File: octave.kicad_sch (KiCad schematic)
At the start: 24 parts, among them Q3 2N3904, Q4 2N3904, Q5 2N3904

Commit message: Actualización de esquemáticos
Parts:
- R10, R11, R12, R13, R14, R15, R16, R17, R18, R19, R2*, R20, R21, R3*: footprint (none) -> Resistor_THT:R_Axial_DIN0207_L6.3mm_D2.5mm_P7.62mm_Horizontal
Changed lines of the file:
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@@
 (kicad_sch
-	(version 20231120)
+	(version 20250114)
 	(generator "eeschema")
-	(generator_version "8.0")
+	(generator_version "9.0")
 	(paper "A4")
 	(junction
@@
 			)
 		)
-		(property "Footprint" ""
+		(property "Footprint" "Resistor_THT:R_Axial_DIN0207_L6.3mm_D2.5mm_P7.62mm_Horizontal"
 			(at 141.732 86.36 90)
 			(effects
@@
 			)
 		)
-		(property "Footprint" ""
+		(property "Footprint" "Resistor_THT:R_Axial_DIN0207_L6.3mm_D2.5mm_P7.62mm_Horizontal"
 			(at 182.372 59.69 90)
 			(effects
@@
 			)
 		)
-		(property "Footprint" ""
+		(property "Footprint" "Resistor_THT:R_Axial_DIN0207_L6.3mm_D2.5mm_P7.62mm_Horizontal"
 			(at 132.08 76.962 90)
 			(effects
@@
 			)
 		)
-		(property "Footprint" ""
+		(property "Footprint" "Resistor_THT:R_Axial_DIN0207_L6.3mm_D2.5mm_P7.62mm_Horizontal"
 			(at 141.732 137.16 90)
 			(effects
@@
 			)
 		)
-		(property "Footprint" ""
+		(property "Footprint" "Resistor_THT:R_Axial_DIN0207_L6.3mm_D2.5mm_P7.62mm_Horizontal"
 			(at 77.978 113.03 90)
 			(effects
@@
 			)
 		)
-		(property "Footprint" ""
+		(property "Footprint" "Resistor_THT:R_Axial_DIN0207_L6.3mm_D2.5mm_P7.62mm_Horizontal"
 			(at 132.08 127.762 90)
 			(effects
@@
 			)
 		)
-		(property "Footprint" ""
+		(property "Footprint" "Resistor_THT:R_Axial_DIN0207_L6.3mm_D2.5mm_P7.62mm_Horizontal"
 			(at 100.838 71.12 90)
 			(effects
@@
 			)
 		)
-		(property "Footprint" ""
+		(property "Footprint" "Resistor_THT:R_Axial_DIN0207_L6.3mm_D2.5mm_P7.62mm_Horizontal"
 			(at 141.732 123.19 90)
 			(effects
@@
 			)
 		)
-		(property "Footprint" ""
+		(property "Footprint" "Resistor_THT:R_Axial_DIN0207_L6.3mm_D2.5mm_P7.62mm_Horizontal"
 			(at 230.378 80.01 90)
 			(effects
@@
 			)
 		)
-		(property "Footprint" ""
+		(property "Footprint" "Resistor_THT:R_Axial_DIN0207_L6.3mm_D2.5mm_P7.62mm_Horizontal"
 			(at 113.538 71.12 90)
 			(effects
@@
 			)
 		)
-		(property "Footprint" ""
+		(property "Footprint" "Resistor_THT:R_Axial_DIN0207_L6.3mm_D2.5mm_P7.62mm_Horizontal"
 			(at 113.538 137.16 90)
 			(effects
@@
 			)
 		)
-		(property "Footprint" ""
+		(property "Footprint" "Resistor_THT:R_Axial_DIN0207_L6.3mm_D2.5mm_P7.62mm_Horizontal"
 			(at 141.732 71.12 90)
 			(effects
@@
 			)
 		)
-		(property "Footprint" ""
+		(property "Footprint" "Resistor_THT:R_Axial_DIN0207_L6.3mm_D2.5mm_P7.62mm_Horizontal"
 			(at 163.322 104.14 90)
 			(effects
@@
 			)
 		)
-		(property "Footprint" ""
+		(property "Footprint" "Resistor_THT:R_Axial_DIN0207_L6.3mm_D2.5mm_P7.62mm_Horizontal"
 			(at 100.838 137.16 90)
 			(effects

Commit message: Actualización esquemáticos
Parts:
- renumbered R2* to R102, R3* to R103
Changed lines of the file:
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@@
 			)
 		)
-		(property "Description" ""
+		(property "Description" "0.2A Ic, 40V Vce, Small Signal NPN Transistor, TO-92"
 			(at 109.22 104.14 0)
 			(effects
@@
 	)
 	(symbol
+		(lib_name "GND_5")
 		(lib_id "power:GND")
 		(at 99.06 142.24 0)
@@
 			)
 		)
-		(property "Description" ""
+		(property "Description" "Power symbol creates a global label with name \"GND\" , ground"
 			(at 99.06 142.24 0)
 			(effects
@@
 			)
 		)
-		(property "Description" ""
+		(property "Description" "Power symbol creates a global label with name \"GND\" , ground"
 			(at 143.51 91.44 0)
 			(effects
@@
 		(dnp no)
 		(fields_autoplaced yes)
-		(property "Reference" "R2*"
-			(at 78.74 111.76 0)
+		(property "Reference" "R102"
+			(at 78.74 111.7599 0)
 			(effects
 				(font
@@
 		)
 		(property "Value" "1M"
-			(at 78.74 114.3 0)
+			(at 78.74 114.2999 0)
 			(effects
 				(font
@@
 			(project "test"
 				(path "/6df9a4de-ce35-4607-9a42-d3c459c15494/3ccfe3c7-9c59-445d-96da-6c8f36b0d39f"
-					(reference "R2*")
+					(reference "R102")
 					(unit 1)
 				)
@@
 	)
 	(symbol
+		(lib_name "GND_4")
 		(lib_id "power:GND")
 		(at 111.76 142.24 0)
@@
 			)
 		)
-		(property "Description" ""
+		(property "Description" "Power symbol creates a global label with name \"GND\" , ground"
 			(at 111.76 142.24 0)
 			(effects
@@
 	)
 	(symbol
+		(lib_name "VCC_1")
 		(lib_id "power:VCC")
 		(at 184.15 53.34 0)
@@
 			)
 		)
-		(property "Description" ""
+		(property "Description" "Power symbol creates a global label with name \"VCC\""
 			(at 184.15 53.34 0)
 			(effects
@@
 	)
 	(symbol
+		(lib_name "VCC_2")
 		(lib_id "power:VCC")
 		(at 143.51 64.77 0)
@@
 			)
 		)
-		(property "Description" ""
+		(property "Description" "Power symbol creates a global label with name \"VCC\""
 			(at 143.51 64.77 0)
 			(effects
@@
 			)
 		)
-		(property "Description" ""
+		(property "Description" "Power symbol creates a global label with name \"GND\" , ground"
 			(at 76.2 120.65 0)
 			(effects
@@
 	)
 	(symbol
+		(lib_name "GND_1")
 		(lib_id "power:GND")
 		(at 203.2 88.9 0)
@@
 			)
 		)
-		(property "Description" ""
+		(property "Description" "Power symbol creates a global label with name \"GND\" , ground"
 			(at 203.2 88.9 0)
 			(effects
@@
 			)
 		)
-		(property "Description" ""
+		(property "Description" "0.2A Ic, 40V Vce, Small Signal NPN Transistor, TO-92"
 			(at 156.21 78.74 0)
 			(effects
@@
 			)
 		)
-		(property "Description" ""
+		(property "Description" "Power symbol creates a global label with name \"VCC\""
 			(at 143.51 116.84 0)
 			(effects
@@
 		(dnp no)
 		(fields_autoplaced yes)
-		(property "Reference" "R3*"
+		(property "Reference" "R103"
 			(at 231.14 78.7399 0)
 			(effects
@@
 			(project "test"
 				(path "/6df9a4de-ce35-4607-9a42-d3c459c15494/3ccfe3c7-9c59-445d-96da-6c8f36b0d39f"
-					(reference "R3*")
+					(reference "R103")
 					(unit 1)
 				)
@@
 			)
 		)
-		(property "Description" ""
+		(property "Description" "Power symbol creates a global label with name \"GND\" , ground"
 			(at 170.18 113.03 0)
 			(effects
@@
 	)
 	(symbol
+		(lib_name "GND_3")
 		(lib_id "power:GND")
 		(at 228.6 88.9 0)
@@
 			)
 		)
-		(property "Description" ""
+		(property "Description" "Power symbol creates a global label with name \"GND\" , ground"
 			(at 228.6 88.9 0)
 			(effects
@@
 	)
 	(symbol
+		(lib_name "GND_2")
 		(lib_id "power:GND")
 		(at 215.9 88.9 0)
@@
 			)
 		)
-		(property "Description" ""
+		(property "Description" "Power symbol creates a global label with name \"GND\" , ground"
 			(at 215.9 88.9 0)
 			(effects
@@
 	)
 	(symbol
+		(lib_name "GND_6")
 		(lib_id "power:GND")
 		(at 143.51 142.24 0)
@@
 			)
 		)
-		(property "Description" ""
+		(property "Description" "Power symbol creates a global label with name \"GND\" , ground"
 			(at 143.51 142.24 0)
 			(effects
@@
 			)
 		)
-		(property "Description" ""
+		(property "Description" "0.2A Ic, 40V Vce, Small Signal NPN Transistor, TO-92"
 			(at 156.21 129.54 0)
 			(effects
@@
 	)
 	(symbol
+		(lib_name "VCC_3")
 		(lib_id "power:VCC")
 		(at 99.06 59.69 0)
@@
 			)
 		)
-		(property "Description" ""
+		(property "Description" "Power symbol creates a global label with name \"VCC\""
 			(at 99.06 59.69 0)
 			(effects

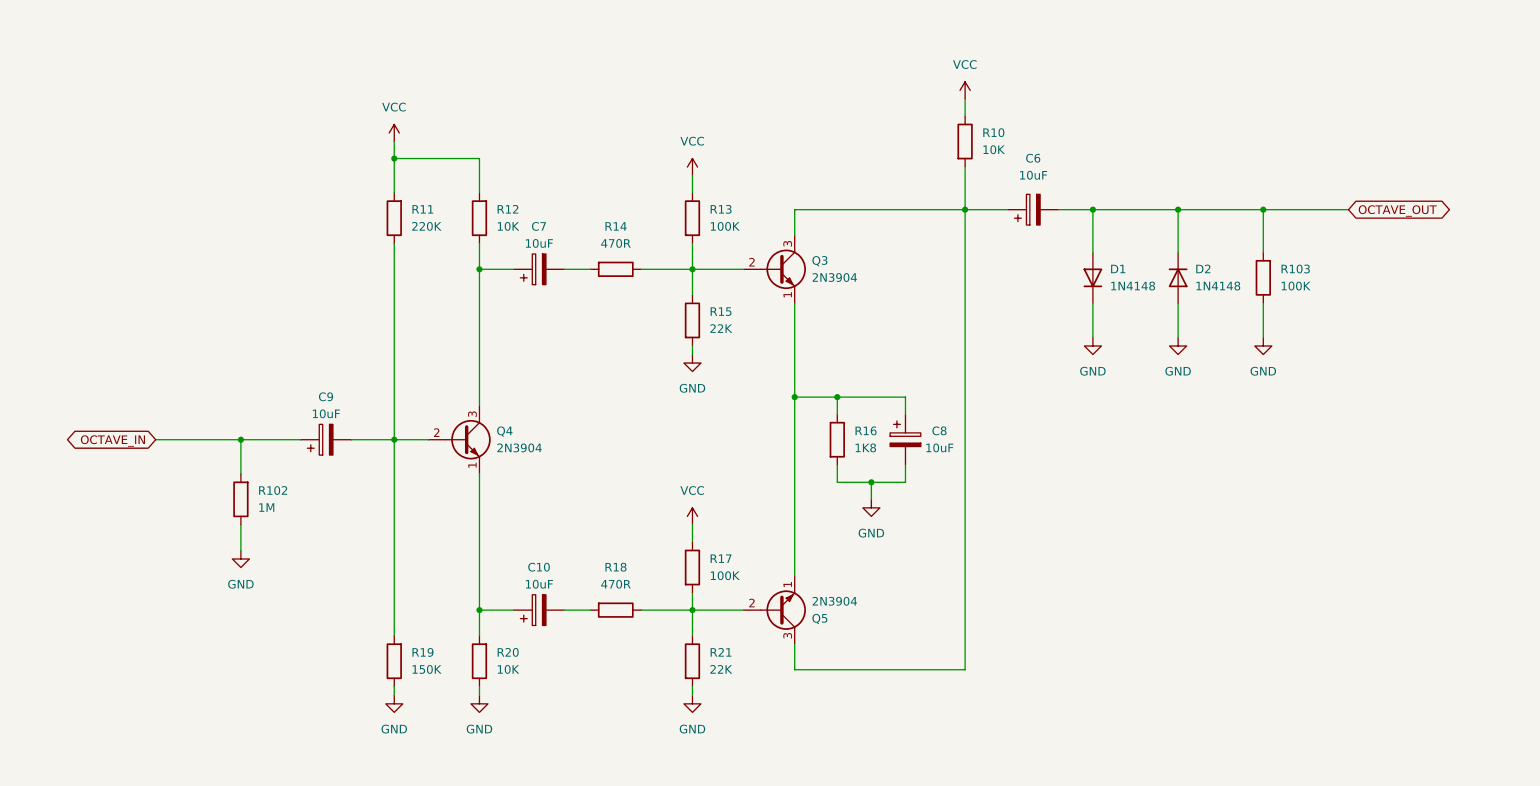
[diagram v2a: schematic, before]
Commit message: Asignación de huellas a componentes.
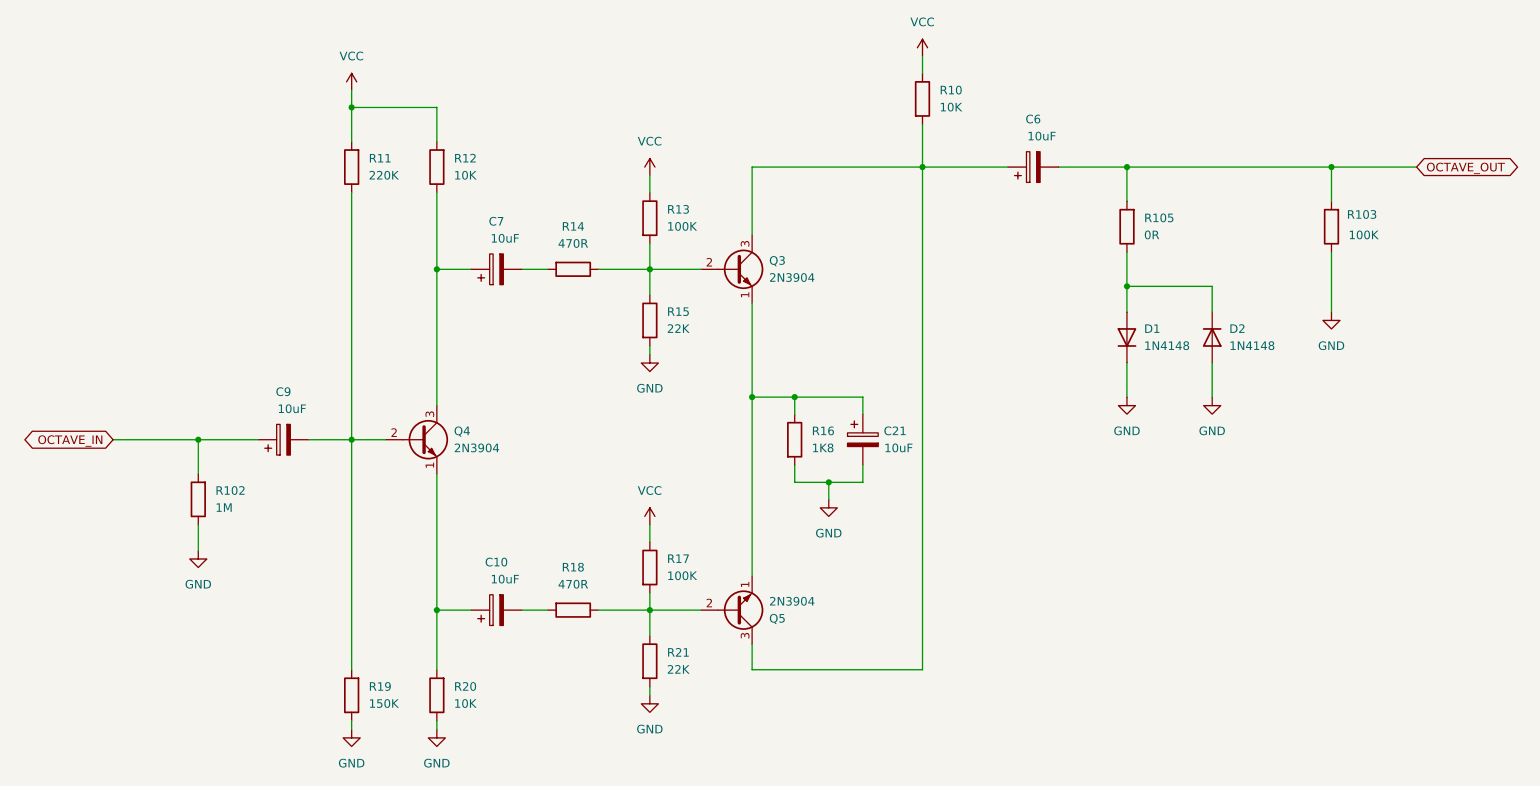
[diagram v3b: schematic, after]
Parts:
- removed C8: 10uF, symbol Device:C_Polarized
- added C21: 10uF, Capacitor_THT:CP_Radial_D5.0mm_P2.00mm, symbol Device:C_Polarized
- added R105: 0R, Resistor_THT:R_Axial_DIN0207_L6.3mm_D2.5mm_P7.62mm_Horizontal, symbol Device:R
- C10, C6, C7, C9: footprint (none) -> Capacitor_THT:CP_Radial_D5.0mm_P2.00mm
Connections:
- net GND: now also C21.2
- net OCTAVE_OUT: now also R105.2; no longer D1.2 (A), D2.1 (K)
- net at Q3.1 (E), Q5.1 (E), R16.1: now also C21.1
- new net: D1.2 (A), D2.1 (K), R105.1
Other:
- moved on the sheet: D1, D2, Q3, Q4, Q5, R10, R102, R103, R11, R12, R13, R14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

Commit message: Adctualización de PCB
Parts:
- D1, D2: footprint Diode_THT:D_DO-35_SOD27_P7.62mm_Horizontal -> DIY_jorge:D_DO-35_SOD27_P7.62mm_Horizontal
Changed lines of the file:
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@@
 			)
 		)
-		(property "Footprint" "Diode_THT:D_DO-35_SOD27_P7.62mm_Horizontal"
+		(property "Footprint" "DIY_jorge:D_DO-35_SOD27_P7.62mm_Horizontal"
 			(at 220.98 88.9 0)
 			(effects
@@
 			)
 		)
-		(property "Footprint" "Diode_THT:D_DO-35_SOD27_P7.62mm_Horizontal"
+		(property "Footprint" "DIY_jorge:D_DO-35_SOD27_P7.62mm_Horizontal"
 			(at 208.28 88.9 0)
 			(effects

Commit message: Finalización de PCB (archivos fabricación pendientes)
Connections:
- net OCTAVE_OUT: now also R105.1; no longer R105.2
- net at D1.2 (A), D2.1 (K): now also R105.2; no longer R105.1
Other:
- moved on the sheet: R105
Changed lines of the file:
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@@
 	(symbol
 		(lib_id "Device:R")
-		(at 208.28 72.39 180)
+		(at 208.28 72.39 0)
 		(unit 1)
 		(exclude_from_sim no)
@@
 					(size 1.27 1.27)
 				)
-				(justify right)
+				(justify left)
 			)
 		)
@@
 					(size 1.27 1.27)
 				)
-				(justify right)
+				(justify left)
 			)
 		)
 		(property "Footprint" "Resistor_THT:R_Axial_DIN0207_L6.3mm_D2.5mm_P7.62mm_Horizontal"
-			(at 210.058 72.39 90)
+			(at 206.502 72.39 90)
 			(effects
 				(font
